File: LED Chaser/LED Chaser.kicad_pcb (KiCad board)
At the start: 2 copper layers, 70.1 x 35.8 mm, 24 parts, among them J1 power in, U1 NE555D, U2 4017

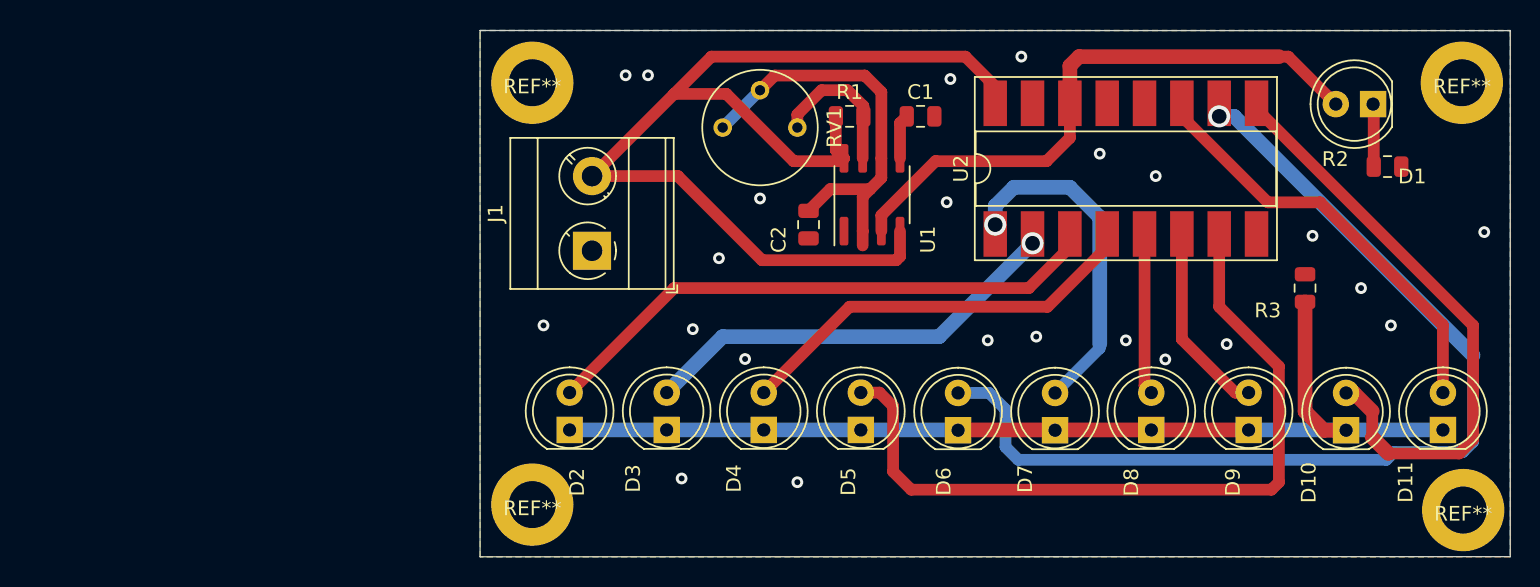
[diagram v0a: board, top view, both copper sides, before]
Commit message: added power supply
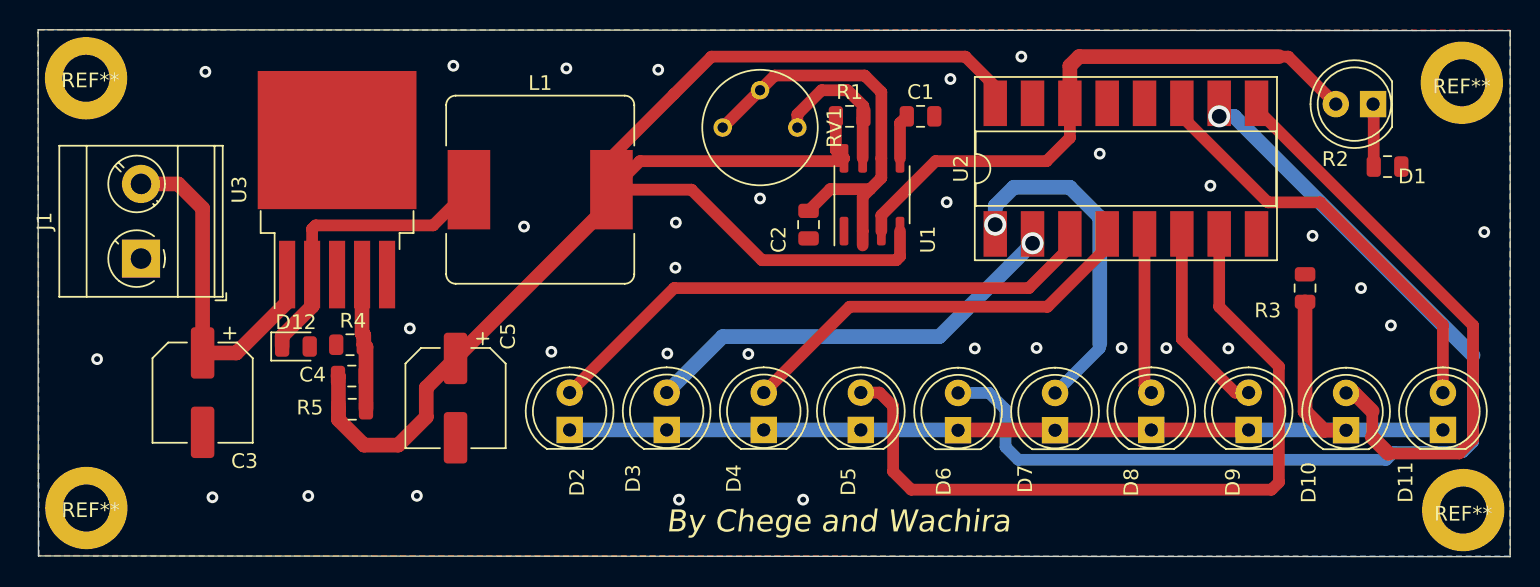
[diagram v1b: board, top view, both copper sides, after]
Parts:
- removed the REF** at (99.8, 80.5)
- removed the REF** at (99.8, 51.8)
- added C3: 27uF, Capacitor_SMD:CP_Elec_6.3x7.7, F.Cu at (77.4, 72.9)
- added C4: 1nF, Capacitor_SMD:C_0805_2012Metric, F.Cu at (87.5, 71.8)
- added C5: 470uF, Capacitor_SMD:CP_Elec_6.3x7.7, F.Cu at (94.6, 73.3)
- added D12: D_Zener, Diode_SMD:D_0805_2012Metric, F.Cu at (83.7, 69.8)
- added L1: 33uH, Inductor_SMD:L_Bourns_SRR1260, F.Cu at (100.4, 59.1)
- added R4: 1k, Resistor_SMD:R_0805_2012Metric, F.Cu at (87.4, 69.6)
- added R5: 3.83k, Resistor_SMD:R_0805_2012Metric, F.Cu at (87.6, 74.0)
- added REF**: MountingHole, MountingHole:MountingHole_3.2mm_M3_DIN965_Pad, F.Cu at (69.5, 51.5)
- added REF**: MountingHole, MountingHole:MountingHole_3.2mm_M3_DIN965_Pad, F.Cu at (69.5, 80.8)
- added U3: LM2596S-ADJ, Package_TO_SOT_SMD:TO-263-5_TabPin3, F.Cu at (86.5, 59.1)
- C1: value C -> 0.01uF
- C2: value C -> 10uF
- R1: value R -> 10k
- R2, R3: value R -> 680R
- RV1: value R_POT -> 10k
- moved J1 30.7 mm to (73.2, 63.8)
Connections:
- J1 pad 2: VCC -> Net-(C3-Pad1)
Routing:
- net VCC: track 74.6 -> 107.5 mm
- net Net-(C3-Pad1): track 0.00 -> 23.8 mm
- net Net-(D12-Pad1): track 0.00 -> 20.6 mm
- net Net-(C4-Pad2): track 0.00 -> 9.28 mm
- net GND: vias 23 -> 32
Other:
- board size 70.1 x 35.8 mm -> 100.2 x 35.9 mm
- board text added: "By Chege and Wachira"
